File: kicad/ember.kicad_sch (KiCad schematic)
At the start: 0 parts

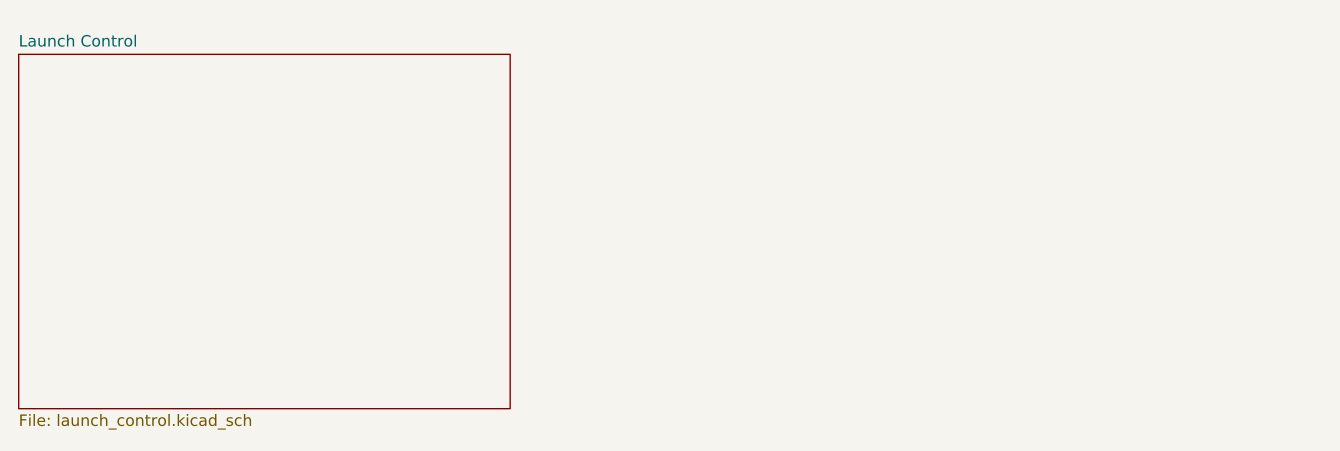
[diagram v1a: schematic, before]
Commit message: added power management for battery
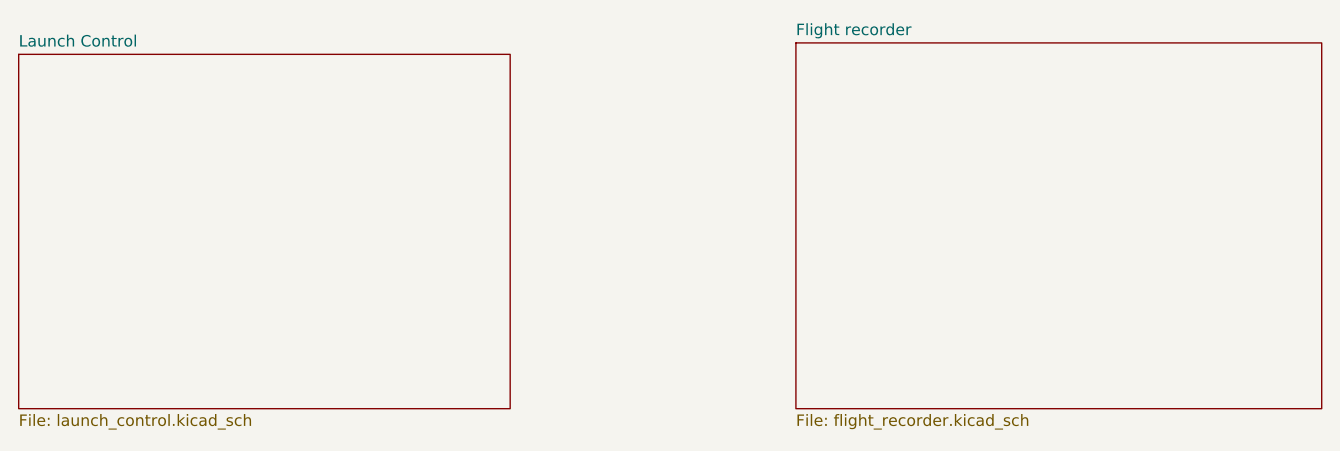
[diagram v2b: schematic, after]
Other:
- added sheet Flight recorder (flight_recorder.kicad_sch)
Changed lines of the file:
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@@
+		)
+	)
+	(sheet
+		(at 107.95 31.75)
+		(size 58.42 40.64)
+		(exclude_from_sim no)
+		(in_bom yes)
+		(on_board yes)
+		(dnp no)
+		(fields_autoplaced yes)
+		(stroke
+			(width 0.1524)
+			(type solid)
+		)
+		(fill
+			(color 0 0 0 0)
+		)
+		(property "Sheetname" "Flight recorder"
+			(at 107.95 31.0384 0)
+			(show_name no)
+			(do_not_autoplace no)
+			(effects
+				(font
+					(size 1.27 1.27)
+				)
+				(justify left bottom)
+			)
+		)
+		(property "Sheetfile" "flight_recorder.kicad_sch"
+			(at 107.95 72.9746 0)
+			(show_name no)
+			(do_not_autoplace no)
+			(effects
+				(font
+					(size 1.27 1.27)
+				)
+				(justify left top)
+			)
+		)
+		(instances
+			(project "ember"
+				(path "/d47a8d18-f726-41c5-b6f5-64829cbcbaae"
+					(page "3")
+				)
+			)
 		)
 	)
